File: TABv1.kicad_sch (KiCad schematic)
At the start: 37 parts, among them J10 Conn_02x03_Odd_Even, J11 Conn_UART_1, J5 Conn_02x06_Counter_Clockwise, J6 SWD, J9 Conn_02x03_Odd_Even, Q2 NMOS, SW2 RESET, U1 RP2350B-QFN80, Y1 12MHz

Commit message: changes sat 13/12/25
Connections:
- net GPIO21 is gone; now on net PWM4: J5.5 (Pin_5)
- net GPIO22 is gone; now on net PWM3: J5.7 (Pin_7)
- net GPIO23 is gone; now on net PWM2: J5.9 (Pin_9)
- net GPIO28 is gone; now on net PWM1: J5.11 (Pin_11)
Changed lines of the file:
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@@
+		)
+	)
+	(label "PWM3"
+		(at 207.01 203.2 180)
+		(effects
+			(font
+				(size 1.27 1.27)
+			)
+			(justify right bottom)
 		)
 	)
@@
 		)
 	)
-	(label "GPIO23"
-		(at 207.01 205.74 180)
-		(effects
-			(font
-				(size 1.27 1.27)
-			)
-			(justify right bottom)
-		)
-	)
 	(label "SCLK"
 		(at 57.15 114.3 0)
@@
 		)
 	)
+	(label "PWM2"
+		(at 207.01 205.74 180)
+		(effects
+			(font
+				(size 1.27 1.27)
+			)
+			(justify right bottom)
+		)
+	)
 	(label "L_BLUE"
 		(at 167.64 170.18 180)
@@
 		)
 	)
+	(label "PWM1"
+		(at 207.01 208.28 180)
+		(effects
+			(font
+				(size 1.27 1.27)
+			)
+			(justify right bottom)
+		)
+	)
 	(label "SCL_RADIO"
 		(at 177.8 254 180)
@@
 		)
 	)
-	(label "GPIO28"
-		(at 207.01 208.28 180)
-		(effects
-			(font
-				(size 1.27 1.27)
-			)
-			(justify right bottom)
-		)
-	)
-	(label "GPIO21"
+	(label "PWM4"
 		(at 207.01 200.66 180)
 		(effects
@@
 		)
 	)
-	(label "GPIO22"
-		(at 207.01 203.2 180)
-		(effects
-			(font
-				(size 1.27 1.27)
-			)
-			(justify right bottom)
-		)
-	)

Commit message: ROBE
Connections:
- net GND: now also J6.1 (Pin_1); no longer J6.3 (Pin_3)
- net at U1.33 (SWCLK): now also J6.2 (Pin_2); no longer J6.1 (Pin_1)
- net at U1.34 (SWDIO): now also J6.3 (Pin_3); no longer J6.2 (Pin_2)
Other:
- moved on the sheet: J6
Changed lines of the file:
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@@
 	(wire
 		(pts
-			(xy 26.67 261.62) (xy 26.67 262.89)
-		)
-		(stroke
-			(width 0)
-			(type default)
-		)
-	)
-	(wire
-		(pts
 			(xy 351.79 237.49) (xy 355.6 237.49)
 		)
@@
 	(wire
 		(pts
+			(xy 22.86 262.89) (xy 26.67 262.89)
+		)
+		(stroke
+			(width 0)
+			(type default)
+		)
+	)
+	(wire
+		(pts
 			(xy 342.9 87.63) (xy 345.44 87.63)
 		)
@@
 	(wire
 		(pts
-			(xy 63.5 157.48) (xy 68.58 157.48)
-		)
-		(stroke
-			(width 0)
-			(type default)
-		)
-	)
-	(wire
-		(pts
 			(xy 121.92 68.58) (xy 124.46 68.58)
 		)
@@
 		)
 	)
+	(wire
+		(pts
+			(xy 67.31 149.86) (xy 63.5 149.86)
+		)
+		(stroke
+			(width 0)
+			(type default)
+		)
+	)
 	(polyline
 		(pts
@@
 	)
 	(label "BUZZ"
-		(at 26.67 261.62 180)
+		(at 22.86 262.89 180)
 		(effects
 			(font
@@
 	(symbol
 		(lib_id "power:GND")
-		(at 68.58 157.48 90)
+		(at 67.31 149.86 90)
 		(unit 1)
 		(exclude_from_sim no)
@@
 		(fields_autoplaced yes)
 		(property "Reference" "#PWR036"
-			(at 74.93 157.48 0)
+			(at 73.66 149.86 0)
 			(effects
 				(font
@@
 		)
 		(property "Value" "GND"
-			(at 72.39 157.4799 90)
+			(at 71.12 149.8599 90)
 			(effects
 				(font
@@
 		)
 		(property "Footprint" ""
-			(at 68.58 157.48 0)
+			(at 67.31 149.86 0)
 			(effects
 				(font
@@
 		)
 		(property "Datasheet" ""
-			(at 68.58 157.48 0)
+			(at 67.31 149.86 0)
 			(effects
 				(font
@@
 		)
 		(property "Description" "Power symbol creates a global label with name \"GND\" , ground"
-			(at 68.58 157.48 0)
+			(at 67.31 149.86 0)
 			(effects
 				(font
@@
 		)
 		(instances
-			(project ""
+			(project "TABv1"
 				(path "/105f6e80-8e20-4d56-8eb3-6fa826818670"
 					(reference "#PWR036")
@@
 	(symbol
 		(lib_id "Connector:Conn_01x03_Pin")
-		(at 58.42 154.94 0)
+		(at 58.42 152.4 0)
 		(unit 1)
 		(exclude_from_sim no)
@@
 		(fields_autoplaced yes)
 		(property "Reference" "J6"
-			(at 59.055 147.32 0)
+			(at 59.055 144.78 0)
 			(effects
 				(font
@@
 		)
 		(property "Value" "SWD"
-			(at 59.055 149.86 0)
+			(at 59.055 147.32 0)
 			(effects
 				(font
@@
 		)
 		(property "Footprint" "Connector_PinHeader_2.54mm:PinHeader_1x03_P2.54mm_Vertical"
-			(at 58.42 154.94 0)
+			(at 58.42 152.4 0)
 			(effects
 				(font
@@
 		)
 		(property "Datasheet" "~"
-			(at 58.42 154.94 0)
+			(at 58.42 152.4 0)
 			(effects
 				(font
@@
 		)
 		(property "Description" "Generic connector, single row, 01x03, script generated"
-			(at 58.42 154.94 0)
+			(at 58.42 152.4 0)
 			(effects
 				(font
@@
 		)
 		(instances
-			(project ""
+			(project "TABv1"
 				(path "/105f6e80-8e20-4d56-8eb3-6fa826818670"
 					(reference "J6")

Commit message: Names fix
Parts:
- C16, C17: value 15p -> 15pf
- RN10: value 220 Ohm -> 220
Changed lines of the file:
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@@
 			)
 		)
-		(property "Value" "15p"
+		(property "Value" "15pf"
 			(at 330.454 236.728 0)
 			(effects
@@
 			)
 		)
-		(property "Value" "15p"
+		(property "Value" "15pf"
 			(at 330.454 224.028 0)
 			(effects
@@
 			)
 		)
-		(property "Value" "220 Ohm"
+		(property "Value" "220"
 			(at 359.41 182.88 90)
 			(effects

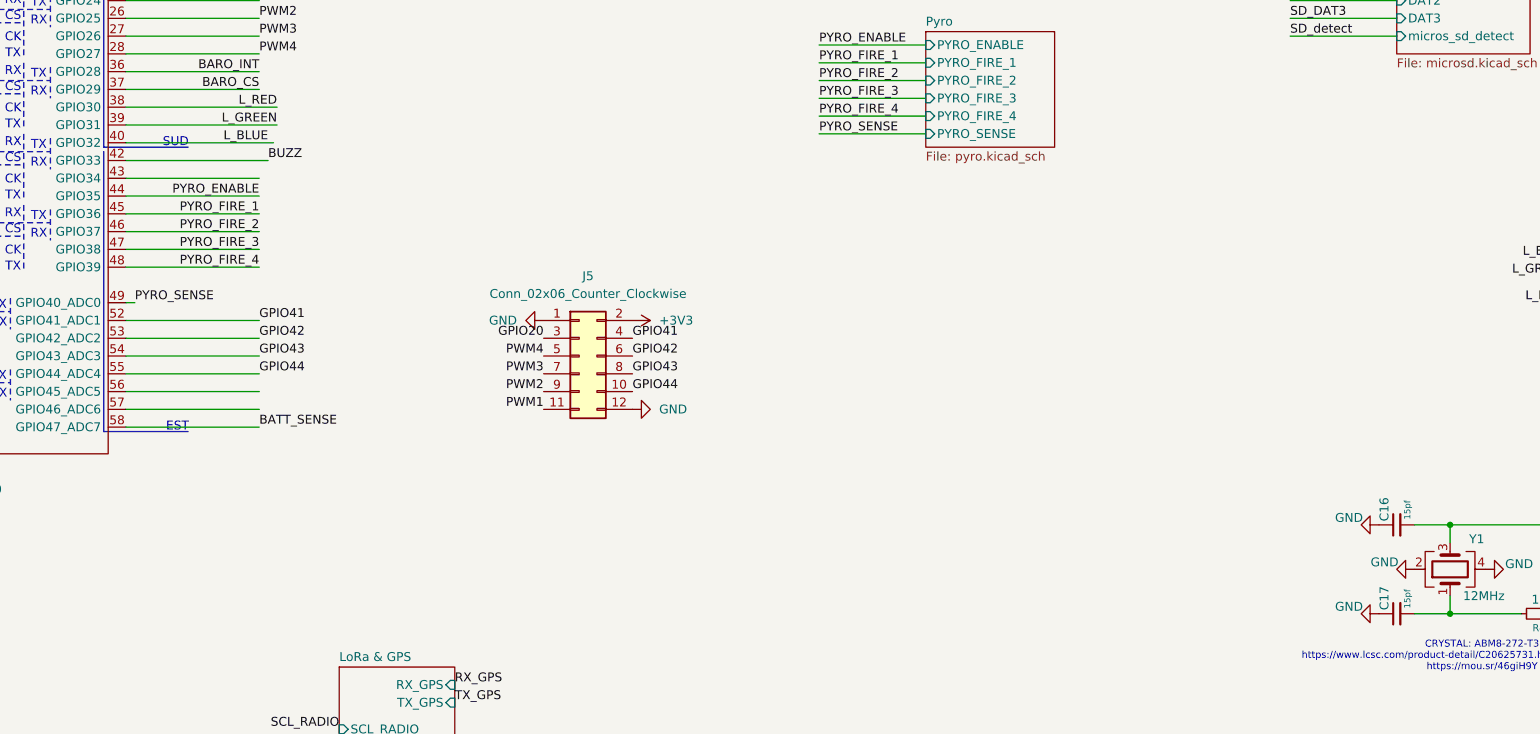
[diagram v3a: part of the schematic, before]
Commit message: 10/01/2025
1v1 fix and v regulator final decision, general BOM corrections and allignments
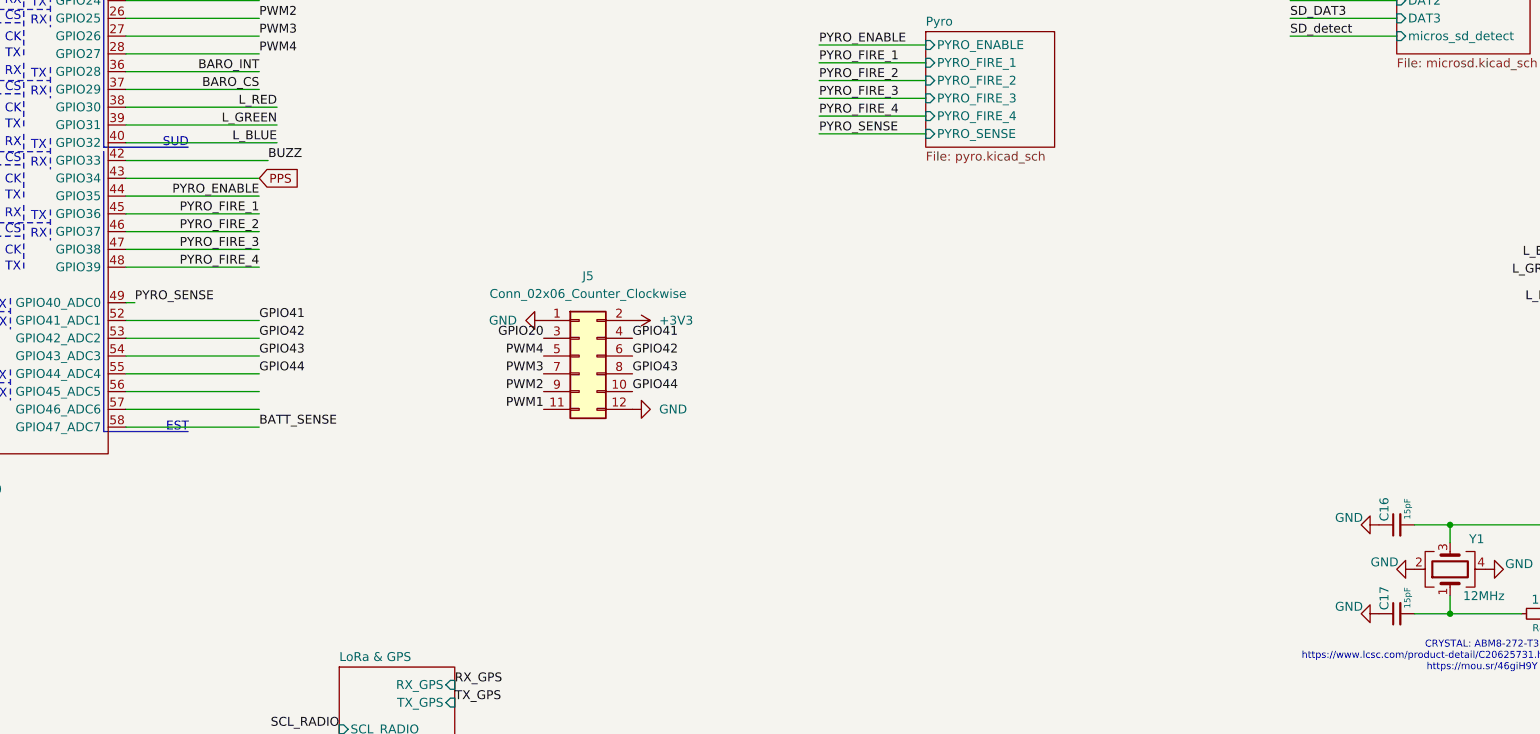
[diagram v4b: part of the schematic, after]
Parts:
- C16, C17: value 15pf -> 15pF
- Q2: footprint Package_TO_SOT_SMD:SOT-23 -> Package_TO_SOT_SMD:SOT-23_Handsoldering
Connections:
- net PPS: now reaches U1.43 (GPIO34)
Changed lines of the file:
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@@
 	(wire
 		(pts
-			(xy 147.32 170.18) (xy 168.402 170.18)
+			(xy 147.32 170.18) (xy 168.91 170.18)
 		)
 		(stroke
@@
 	)
 	(label "L_BLUE"
-		(at 167.64 170.18 180)
+		(at 168.91 170.18 180)
 		(effects
 			(font
@@
 		)
 	)
+	(global_label "PPS"
+		(shape input)
+		(at 166.37 175.26 0)
+		(fields_autoplaced yes)
+		(effects
+			(font
+				(size 1.27 1.27)
+			)
+			(justify left)
+		)
+		(property "Intersheetrefs" "${INTERSHEET_REFS}"
+			(at 173.1047 175.26 0)
+			(effects
+				(font
+					(size 1.27 1.27)
+				)
+				(justify left)
+				(hide yes)
+			)
+		)
+	)
 	(global_label "D-"
 		(shape input)
@@
 			)
 		)
-		(property "Value" "15pf"
+		(property "Value" "15pF"
 			(at 330.454 236.728 0)
 			(effects
@@
 			)
 		)
-		(property "Footprint" "Package_TO_SOT_SMD:SOT-23"
+		(property "Footprint" "Package_TO_SOT_SMD:SOT-23_Handsoldering"
 			(at 45.72 260.35 0)
 			(effects
@@
 			)
 		)
-		(property "Value" "15pf"
+		(property "Value" "15pF"
 			(at 330.454 224.028 0)
 			(effects

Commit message: Small changes
modified Main LEDs.
Added Radio LEDs.

Connected the GPS uart to the Radio.
Added a test point for the GPS PRG pin.

Modified the Pyro current limiter for better BOM compliance.

Modified a copule of estetic things on the schematic.
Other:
- note added: "Connectors"
- note added: "LED"
- note added: "Oscillator Crystal"
- note added: "Speaker + Amplifier"
- moved on the sheet: C10, C11, C12, C13, C14, C15, C5, C6, C7, C8, C9, D5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

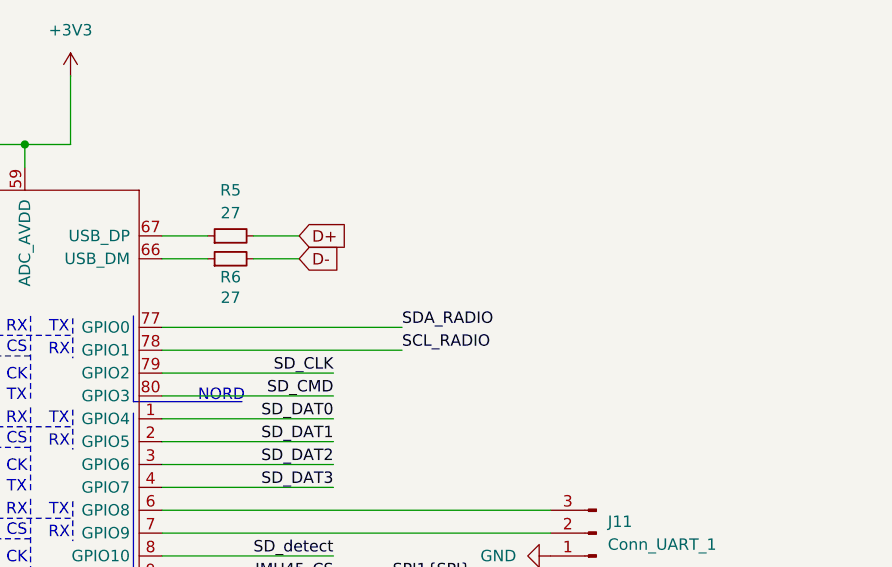
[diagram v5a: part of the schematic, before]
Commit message: Last fixes
Added i2c connection to gps.
Added test point for swd and Uart for radio.
check footprint compatibility between liv3f and liv4f.
... Other ...
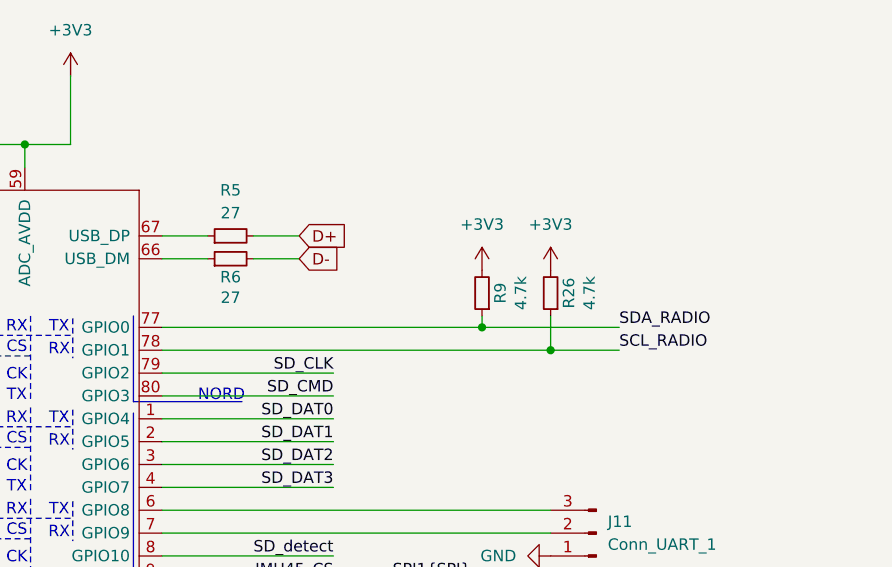
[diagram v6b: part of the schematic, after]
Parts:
- added R26, R9: 4.7k, Resistor_SMD:R_0603_1608Metric_Pad0.98x0.95mm_HandSolder, symbol Device:R_Small
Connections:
- net +3V3: now also R26.2, R9.2
- net SCL_RADIO: now also R26.1
- net SDA_RADIO: now also R9.1
